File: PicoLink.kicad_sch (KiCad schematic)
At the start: 14 parts, among them J1 USB_C_Receptacle_USB2.0_16P, SW1 SW_Push, U1 RP2040, Y1 12MHz

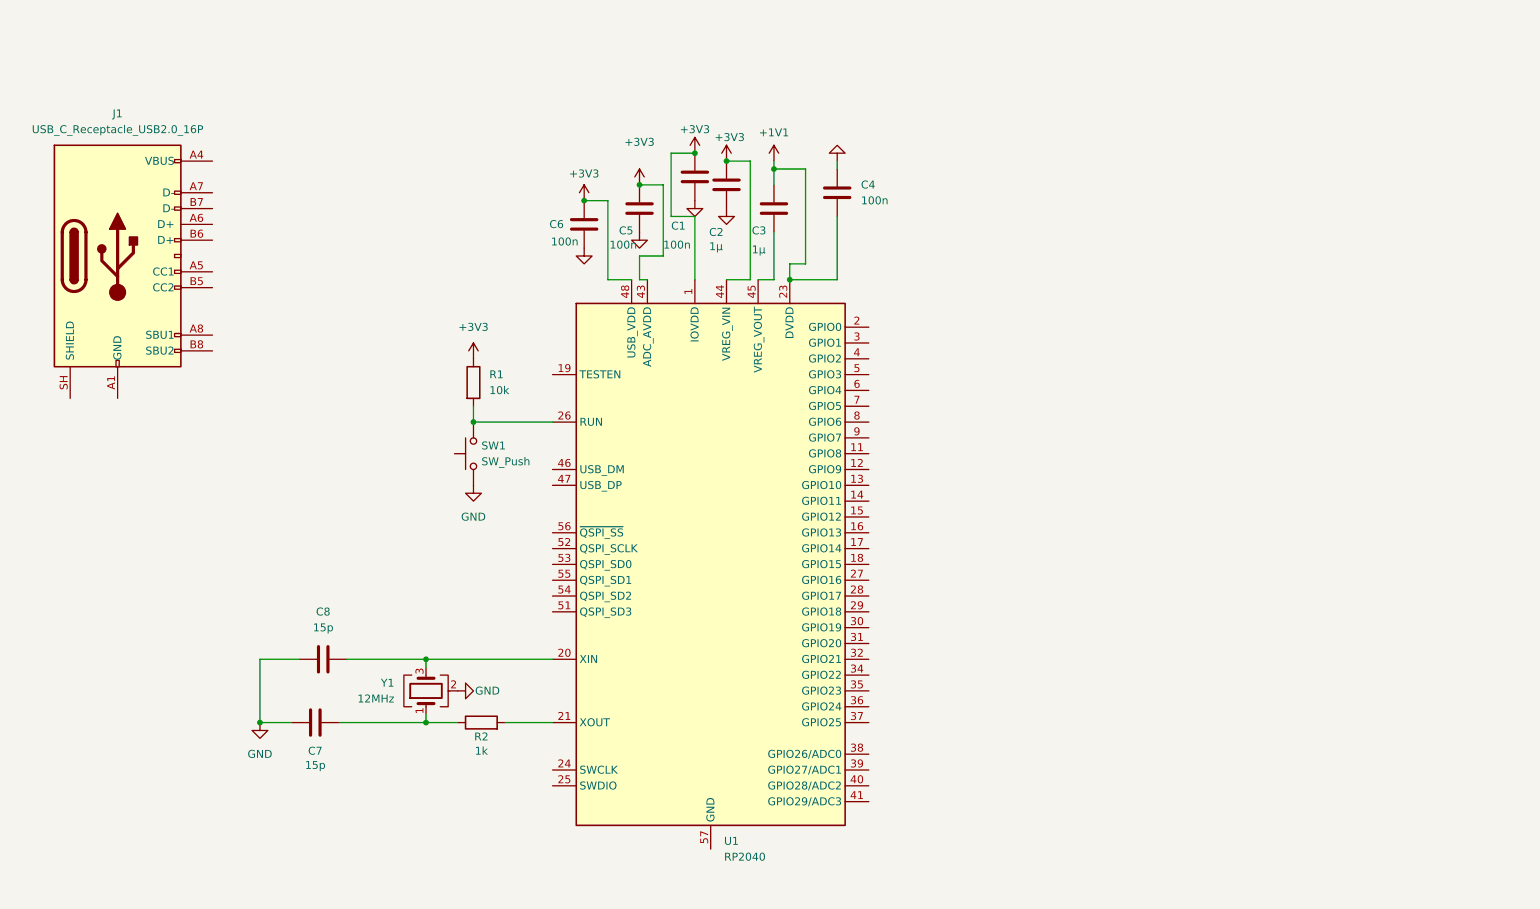
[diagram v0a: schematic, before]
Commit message: Added footprints
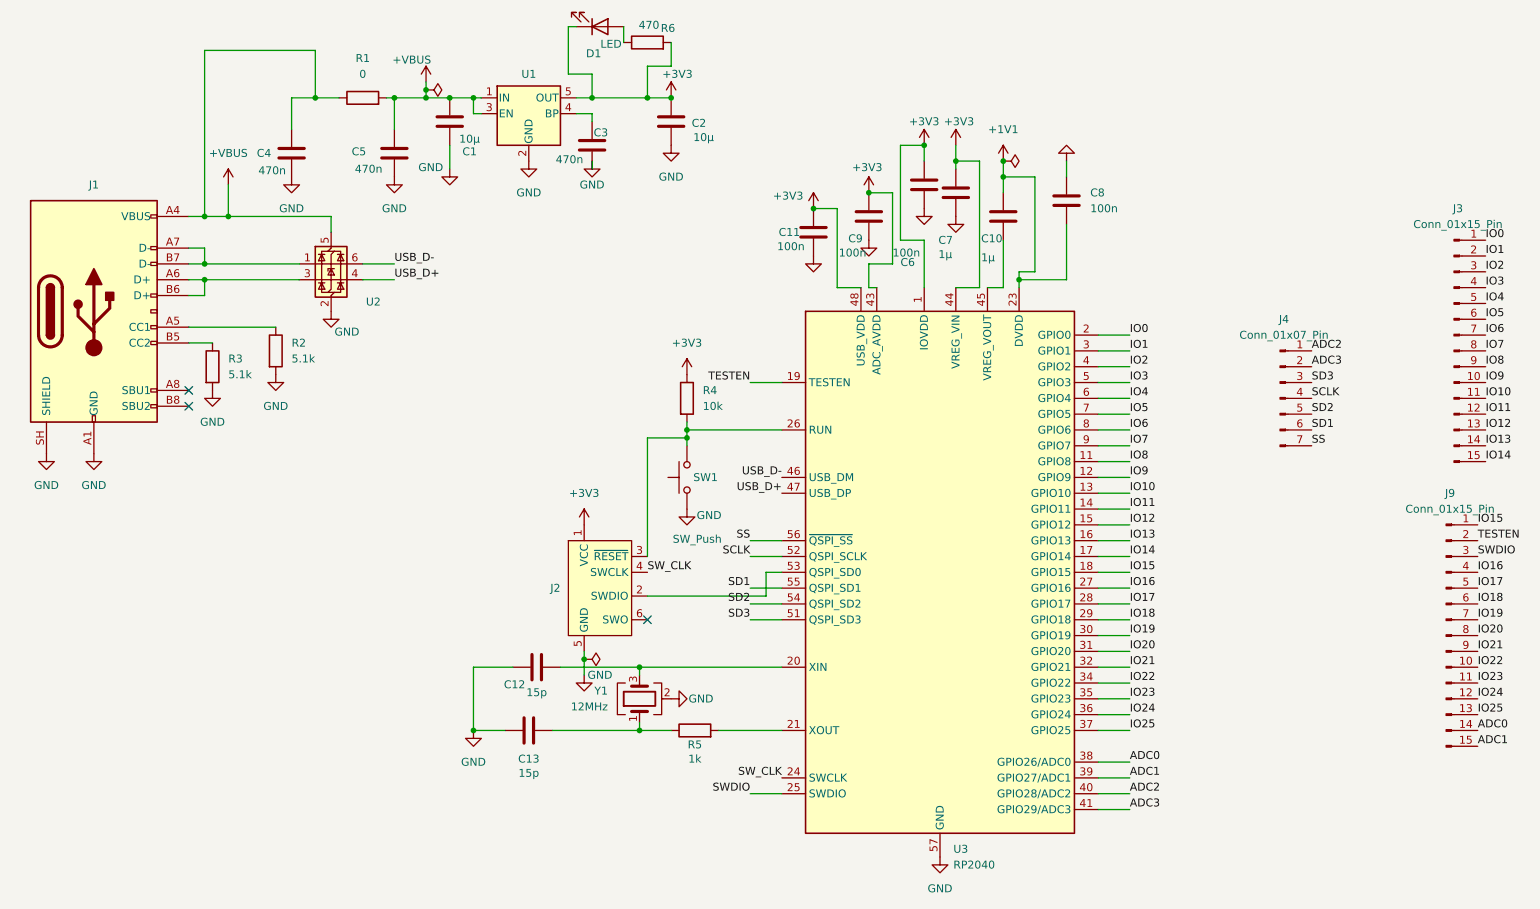
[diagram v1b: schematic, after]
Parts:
- added C1, C2: 10µ, Capacitor_SMD:C_0603_1608Metric, symbol Device:C
- added C3, C4, C5: 470n, Capacitor_SMD:C_0603_1608Metric, symbol Device:C
- added D1: LED, LED_SMD:LED_0805_2012Metric, symbol Device:LED
- added J2: Conn_ARM_SWD_TagConnect_TC2030, Connector:Tag-Connect_TC2030-IDC-FP_2x03_P1.27mm_Vertical, symbol Connector:Conn_ARM_SWD_TagConnect_TC2030
- added J3, J9: Conn_01x15_Pin, Connector_PinHeader_2.54mm:PinHeader_1x15_P2.54mm_Vertical, symbol Connector:Conn_01x15_Pin
- added J4: Conn_01x07_Pin, Connector_PinHeader_2.54mm:PinHeader_1x07_P2.54mm_Vertical, symbol Connector:Conn_01x07_Pin
- added R1: 0, Resistor_SMD:R_0603_1608Metric, symbol Device:R
- added R2, R3: 5.1k, Resistor_SMD:R_0603_1608Metric, symbol Device:R
- added R6: 470, Resistor_SMD:R_0603_1608Metric, symbol Device:R
- added U1: SPX3819M5-L-3-3, Package_TO_SOT_SMD:SOT-23-5, symbol Regulator_Linear:SPX3819M5-L-3-3
- added U2: USBLC6-2SC6, Package_TO_SOT_SMD:SOT-23-6, symbol Power_Protection:USBLC6-2SC6
- C10: renamed from C3; footprint (none) -> Capacitor_SMD:C_0603_1608Metric
- C11: renamed from C6; footprint (none) -> Capacitor_SMD:C_0603_1608Metric
- C12: renamed from C8; footprint (none) -> Capacitor_SMD:C_0603_1608Metric
- C13: renamed from C7; footprint (none) -> Capacitor_SMD:C_0603_1608Metric
- C6: renamed from C1; footprint (none) -> Capacitor_SMD:C_0603_1608Metric
- C7: renamed from C2; footprint (none) -> Capacitor_SMD:C_0603_1608Metric
- C8: renamed from C4; footprint (none) -> Capacitor_SMD:C_0603_1608Metric
- C9: renamed from C5; footprint (none) -> Capacitor_SMD:C_0603_1608Metric
- J1: footprint (none) -> Connector_USB:USB_C_Receptacle_G-Switch_GT-USB-7010ASV
- R4: renamed from R1; footprint (none) -> Resistor_SMD:R_0603_1608Metric
- R5: renamed from R2; footprint (none) -> Resistor_SMD:R_0603_1608Metric
- SW1: footprint (none) -> Button_Switch_SMD:SW_SPST_B3U-1000P
- Y1: footprint (none) -> Crystal:Crystal_SMD_5032-4Pin_5.0x3.2mm
- renumbered U1 to U3
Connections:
- net +3V3: now also C2.1, D1.1 (K), J2.1 (VCC), R6.2, U1.5 (OUT)
- net GND: now also J1.A1 (GND), J1.A12 (GND), J1.B1 (GND), J1.B12 (GND), J1.SH (SHIELD), U3.57 (GND), C1.2, C2.2, C3.2, C4.2, C5.2, J2.5 (GND), R2.2, R3.2, U1.2 (GND), U2.2 (GND)
- net at R4.2, SW1.2, U3.26 (RUN): now also J2.3 (~{RESET})
- net +VBUS: now reaches J1.A4 (VBUS), J1.A9 (VBUS), J1.B4 (VBUS), J1.B9 (VBUS)
- net +VBUS: now also C1.1, C4.1, C5.1, R1.1, R1.2, U1.1 (IN), U1.3 (EN), U2.5 (VBUS)
- net at J1.A5 (CC1): now also R2.1
- net at J1.A6 (D+): now also J1.B6 (D+), U2.3 (I/O2)
- net at J1.A7 (D-): now also J1.B7 (D-), U2.1 (I/O1)
- net at J1.B5 (CC2): now also R3.1
- net IO8: now reaches U3.11 (GPIO8)
- net IO8: now also J3.9 (Pin_9)
- net IO9: now reaches U3.12 (GPIO9)
- net IO9: now also J3.10 (Pin_10)
- net IO10: now reaches U3.13 (GPIO10)
- net IO10: now also J3.11 (Pin_11)
- net IO11: now reaches U3.14 (GPIO11)
- net IO11: now also J3.12 (Pin_12)
- net IO12: now reaches U3.15 (GPIO12)
- net IO12: now also J3.13 (Pin_13)
- net IO13: now reaches U3.16 (GPIO13)
- net IO13: now also J3.14 (Pin_14)
- net IO14: now reaches U3.17 (GPIO14)
- net IO14: now also J3.15 (Pin_15)
- net IO15: now reaches U3.18 (GPIO15)
- net IO15: now also J9.1 (Pin_1)
- net TESTEN: now reaches U3.19 (TESTEN)
- net TESTEN: now also J9.2 (Pin_2)
- net IO0: now reaches U3.2 (GPIO0)
- net IO0: now also J3.1 (Pin_1)
- net SW_CLK: now reaches U3.24 (SWCLK)
- net SW_CLK: now also J2.4 (SWCLK)
- net SWDIO: now reaches U3.25 (SWDIO)
- net SWDIO: now also J9.3 (Pin_3)
- net IO16: now reaches U3.27 (GPIO16)
- net IO16: now also J9.4 (Pin_4)
- net IO17: now reaches U3.28 (GPIO17)
- net IO17: now also J9.5 (Pin_5)
- net IO18: now reaches U3.29 (GPIO18)
- net IO18: now also J9.6 (Pin_6)
- net IO1: now reaches U3.3 (GPIO1)
- net IO1: now also J3.2 (Pin_2)
- net IO19: now reaches U3.30 (GPIO19)
- net IO19: now also J9.7 (Pin_7)
- net IO20: now reaches U3.31 (GPIO20)
- net IO20: now also J9.8 (Pin_8)
- net IO21: now reaches U3.32 (GPIO21)
- net IO21: now also J9.9 (Pin_9)
- net IO22: now reaches U3.34 (GPIO22)
- net IO22: now also J9.10 (Pin_10)
- net IO23: now reaches U3.35 (GPIO23)
- net IO23: now also J9.11 (Pin_11)
- net IO24: now reaches U3.36 (GPIO24)
- net IO24: now also J9.12 (Pin_12)
- net IO25: now reaches U3.37 (GPIO25)
- net IO25: now also J9.13 (Pin_13)
- net ADC0: now reaches U3.38 (GPIO26/ADC0)
- net ADC0: now also J9.14 (Pin_14)
- net ADC1: now reaches U3.39 (GPIO27/ADC1)
- net ADC1: now also J9.15 (Pin_15)
- net IO2: now reaches U3.4 (GPIO2)
- net IO2: now also J3.3 (Pin_3)
- net ADC2: now reaches U3.40 (GPIO28/ADC2)
- net ADC2: now also J4.1 (Pin_1)
- net ADC3: now reaches U3.41 (GPIO29/ADC3)
- net ADC3: now also J4.2 (Pin_2)
- net USB_D-: now reaches U3.46 (USB_DM)
- net USB_D-: now also U2.6 (I/O1)
- net USB_D+: now reaches U3.47 (USB_DP)
- net USB_D+: now also U2.4 (I/O2)
- net IO3: now reaches U3.5 (GPIO3)
- net IO3: now also J3.4 (Pin_4)
- net SD3: now reaches U3.51 (QSPI_SD3)
- net SD3: now also J4.3 (Pin_3)
- net SCLK: now reaches U3.52 (QSPI_SCLK)
- net SCLK: now also J4.4 (Pin_4)
- net at U3.53 (QSPI_SD0): now also J2.2 (SWDIO)
- net SD2: now reaches U3.54 (QSPI_SD2)
- net SD2: now also J4.5 (Pin_5)
- net SD1: now reaches U3.55 (QSPI_SD1)
- net SD1: now also J4.6 (Pin_6)
- net SS: now reaches U3.56 (~{QSPI_SS})
- net SS: now also J4.7 (Pin_7)
- net IO4: now reaches U3.6 (GPIO4)
- net IO4: now also J3.5 (Pin_5)
- net IO5: now reaches U3.7 (GPIO5)
- net IO5: now also J3.6 (Pin_6)
- net IO6: now reaches U3.8 (GPIO6)
- net IO6: now also J3.7 (Pin_7)
- net IO7: now reaches U3.9 (GPIO7)
- net IO7: now also J3.8 (Pin_8)
- new net: D1.2 (A), R6.1
- new net: C3.1, U1.4 (BP)
- no-connect marks 0 -> 3
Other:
- moved on the sheet: C10, C11, C12, C13, C6, C7, C8, C9, J1, R4, R5, SW1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
